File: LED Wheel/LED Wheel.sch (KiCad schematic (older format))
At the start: 0 parts

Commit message: Init Commit
Initial Commit with the Near-Finished Board Layout
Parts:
- added H1, H2, H3: MountingHole, MountingHole:MountingHole_2.2mm_M2, symbol Mechanical:MountingHole
- added J1, J2, J3: I/O, Connector_PinHeader_1.27mm:PinHeader_1x08_P1.27mm_Vertical, symbol Connector_Generic:Conn_01x08
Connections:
- new net +12V: J1.1 (Pin_1), J2.1 (Pin_1), J3.1 (Pin_1)
- new net GND: J1.8 (Pin_8), J2.8 (Pin_8), J3.8 (Pin_8)
- new net SPI1_CLK: J1.5 (Pin_5), J2.5 (Pin_5), J3.5 (Pin_5)
- new net SPI1_MISO: J1.4 (Pin_4), J2.4 (Pin_4), J3.4 (Pin_4)
- new net SPI1_MOSI: J1.3 (Pin_3), J2.3 (Pin_3), J3.3 (Pin_3)
- new net ~0E~: J1.6 (Pin_6), J2.6 (Pin_6), J3.6 (Pin_6)
- new net ~CS~_BLUE: J1.2 (Pin_2)
- new net ~CS~_GREEN: J3.2 (Pin_2)
- new net ~CS~_RED: J2.2 (Pin_2)
- new net ~RESET~: J1.7 (Pin_7), J2.7 (Pin_7), J3.7 (Pin_7)

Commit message: Rev A0 Commit
Files all sent to PCB manufacturer & BOM
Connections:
- net ~CS~_GREEN is gone; now on net Blue LED Controller/~OE~: J3.2 (Pin_2)
- net ~CS~_RED is gone; now on net Blue LED Controller/~OE~: J2.2 (Pin_2)
- net SPI1_CLK renamed Blue LED Controller/SPI1_CLK
- net SPI1_MISO renamed Blue LED Controller/~RESET~
- removed net SPI1_MOSI: J1.3 (Pin_3), J2.3 (Pin_3), J3.3 (Pin_3)
- net ~0E~ renamed Blue LED Controller/SPI1_MOSI
- net ~CS~_BLUE renamed Blue LED Controller/~OE~
- net ~RESET~ renamed Blue LED Controller/SPI1_MISO
- new net Blue LED Controller/~CS~_BLUE: J1.3 (Pin_3)
- new net Green LED Controller/~CS~_GREEN: J3.3 (Pin_3)
- new net Red LED Controller/~CS~_RED: J2.3 (Pin_3)
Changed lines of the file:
@@
 F0 "Green LED Controller" 50
 F1 "G_LED_Controller.sch" 50
-F2 "SPI1_MOSI" I L 4500 6050 50
+F2 "SPI1_MOSI" I L 4500 6350 50
 F3 "SPI1_CLK" I L 4500 6250 50
-F4 "~OE~" I L 4500 6350 50
-F5 "~RESET~" I L 4500 6450 50
-F6 "SPI1_MISO" O L 4500 6150 50
-F7 "~CS~_GREEN" I L 4500 5950 50
+F4 "~OE~" I L 4500 5950 50
+F5 "~RESET~" I L 4500 6150 50
+F6 "SPI1_MISO" O L 4500 6450 50
+F7 "~CS~_GREEN" I L 4500 6050 50
 F8 "G_12V" I L 4500 5725 50
 F9 "G_GND" I L 4500 6675 50
@@
 F0 "Red LED Controller" 50
 F1 "R_LED_Controller.sch" 50
-F2 "SPI1_MOSI" I L 4525 4400 50
+F2 "SPI1_MOSI" I L 4525 4700 50
 F3 "SPI1_CLK" I L 4525 4600 50
-F4 "~OE~" I L 4525 4700 50
-F5 "~RESET~" I L 4525 4800 50
-F6 "SPI1_MISO" O L 4525 4500 50
-F7 "~CS~_RED" I L 4525 4300 50
+F4 "~OE~" I L 4525 4300 50
+F5 "~RESET~" I L 4525 4500 50
+F6 "SPI1_MISO" O L 4525 4800 50
+F7 "~CS~_RED" I L 4525 4400 50
 F8 "R_GND" I L 4525 5025 50
 F9 "R_12V" I L 4525 4075 50
@@
 Wire Wire Line
 	4200 3400 4525 3400
-Wire Wire Line
-	2850 2675 2950 2675
-Wire Wire Line
-	2850 2775 3425 2775
-Wire Wire Line
-	2850 2875 3500 2875
-Wire Wire Line
-	2850 2975 3575 2975
-Wire Wire Line
-	2850 3075 3650 3075
-Wire Wire Line
-	2850 3175 3725 3175
 Wire Wire Line
 	4200 3400 4200 3275
@@
 F0 "Blue LED Controller" 50
 F1 "B_LED_Controller.sch" 50
-F2 "~CS~_BLUE" I L 4525 2675 50
-F3 "SPI1_MOSI" I L 4525 2775 50
+F2 "~CS~_BLUE" I L 4525 2775 50
+F3 "SPI1_MOSI" I L 4525 3075 50
 F4 "SPI1_CLK" I L 4525 2975 50
-F5 "~OE~" I L 4525 3075 50
-F6 "~RESET~" I L 4525 3175 50
-F7 "SPI1_MISO" O L 4525 2875 50
+F5 "~OE~" I L 4525 2675 50
+F6 "~RESET~" I L 4525 2875 50
+F7 "SPI1_MISO" O L 4525 3175 50
 F8 "B_12V" I L 4525 2450 50
 F9 "B_GND" I L 4525 3400 50
@@
 $EndComp
 Wire Wire Line
-	2850 4300 2950 4300
-Wire Wire Line
-	4525 4400 3425 4400
-Wire Wire Line
-	2850 4500 3500 4500
-Wire Wire Line
-	2850 4600 3575 4600
-Wire Wire Line
-	4525 4700 3650 4700
-Wire Wire Line
-	4525 4800 3725 4800
-Wire Wire Line
-	2850 4900 4200 4900
-Wire Wire Line
 	4200 5025 4525 5025
 Wire Wire Line
@@
 $EndComp
 Wire Wire Line
-	2825 5950 2950 5950
-Wire Wire Line
-	4500 6050 3425 6050
-Wire Wire Line
-	2825 6150 3500 6150
-Wire Wire Line
-	2825 6250 3575 6250
-Wire Wire Line
-	4500 6350 3650 6350
-Wire Wire Line
-	4500 6450 3725 6450
-Wire Wire Line
 	2825 6550 4175 6550
 Wire Wire Line
@@
 	4175 5625 4175 5725
 Connection ~ 4175 5725
-Wire Wire Line
-	3425 2775 3425 4400
-Connection ~ 3425 2775
-Wire Wire Line
-	3425 2775 4525 2775
-Connection ~ 3425 4400
-Wire Wire Line
-	3425 4400 2850 4400
-Wire Wire Line
-	3425 4400 3425 6050
-Connection ~ 3425 6050
-Wire Wire Line
-	3425 6050 2825 6050
-Wire Wire Line
-	3500 2875 3500 4500
-Connection ~ 3500 2875
-Wire Wire Line
-	3500 2875 4525 2875
-Connection ~ 3500 4500
-Wire Wire Line
-	3500 4500 4525 4500
-Wire Wire Line
-	3500 4500 3500 6150
-Connection ~ 3500 6150
-Wire Wire Line
-	3500 6150 4500 6150
-Wire Wire Line
-	3575 2975 3575 4600
-Connection ~ 3575 2975
-Wire Wire Line
-	3575 2975 4525 2975
-Connection ~ 3575 4600
-Wire Wire Line
-	3575 4600 4525 4600
-Wire Wire Line
-	3575 4600 3575 6250
-Connection ~ 3575 6250
-Wire Wire Line
-	3575 6250 4500 6250
-Wire Wire Line
-	3650 3075 3650 4700
-Connection ~ 3650 3075
-Wire Wire Line
-	3650 3075 4525 3075
-Connection ~ 3650 4700
-Wire Wire Line
-	3650 4700 2850 4700
-Wire Wire Line
-	3650 4700 3650 6350
-Connection ~ 3650 6350
-Wire Wire Line
-	3650 6350 2825 6350
-Wire Wire Line
-	3725 3175 3725 4800
-Connection ~ 3725 3175
-Wire Wire Line
-	3725 3175 4525 3175
-Connection ~ 3725 4800
-Wire Wire Line
-	3725 4800 2850 4800
-Wire Wire Line
-	3725 4800 3725 6450
-Connection ~ 3725 6450
-Wire Wire Line
-	3725 6450 2825 6450
-Text GLabel 2775 3425 0    50   Input ~ 0
-~CS~_BLUE
-Wire Wire Line
-	2775 3425 2950 3425
-Wire Wire Line
-	2950 3425 2950 2675
-Connection ~ 2950 2675
-Wire Wire Line
-	2950 2675 4525 2675
-Text GLabel 2775 5050 0    50   Input ~ 0
-~CS~_RED
-Wire Wire Line
-	2775 5050 2950 5050
-Wire Wire Line
-	2950 5050 2950 4300
-Connection ~ 2950 4300
-Wire Wire Line
-	2950 4300 4525 4300
-Text GLabel 2775 6700 0    50   Input ~ 0
-~CS~_GREEN
-Wire Wire Line
-	2775 6700 2950 6700
-Wire Wire Line
-	2950 6700 2950 5950
-Text GLabel 3025 2250 0    50   Input ~ 0
-SPI1_MOSI
-Wire Wire Line
-	3025 2250 3425 2250
-Wire Wire Line
-	3425 2250 3425 2775
-Text GLabel 3025 2150 0    50   Input ~ 0
-SPI1_MISO
-Wire Wire Line
-	3025 2150 3500 2150
-Wire Wire Line
-	3500 2150 3500 2875
-Connection ~ 2950 5950
-Wire Wire Line
-	2950 5950 4500 5950
-Text GLabel 3025 2050 0    50   Input ~ 0
-SPI1_CLK
-Text GLabel 3025 1950 0    35   Input ~ 0
-~0E~
-Text GLabel 3025 1850 0    35   Input ~ 0
-~RESET~
-Wire Wire Line
-	3025 1850 3725 1850
-Wire Wire Line
-	3725 1850 3725 3175
-Wire Wire Line
-	3650 3075 3650 1950
-Wire Wire Line
-	3650 1950 3025 1950
-Wire Wire Line
-	3025 2050 3575 2050
-Wire Wire Line
-	3575 2050 3575 2975
 $Comp
 L Mechanical:MountingHole H1
@@
 	1    0    0    -1
 $EndComp
+Wire Wire Line
+	2850 4900 4200 4900
+Wire Wire Line
+	2850 2775 4525 2775
+Wire Wire Line
+	2850 4400 4525 4400
+Wire Wire Line
+	2825 6050 4500 6050
+Wire Wire Line
+	3575 6250 4500 6250
+Wire Wire Line
+	2825 6250 3575 6250
+Connection ~ 3575 6250
+Wire Wire Line
+	2850 4600 3575 4600
+Wire Wire Line
+	3575 4600 4525 4600
+Connection ~ 3575 4600
+Wire Wire Line
+	3575 4600 3575 6250
+Wire Wire Line
+	3500 6150 4500 6150
+Wire Wire Line
+	2825 6150 3500 6150
+Connection ~ 3500 6150
+Wire Wire Line
+	3500 4500 4525 4500
+Wire Wire Line
+	2850 4500 3500 4500
+Connection ~ 3500 4500
+Wire Wire Line
+	3500 4500 3500 6150
+Wire Wire Line
+	3725 6450 4500 6450
+Wire Wire Line
+	2825 6450 3725 6450
+Connection ~ 3725 6450
+Wire Wire Line
+	3725 4800 4525 4800
+Wire Wire Line
+	2850 4800 3725 4800
+Connection ~ 3725 4800
+Wire Wire Line
+	3725 4800 3725 6450
+Wire Wire Line
+	3650 6350 4500 6350
+Wire Wire Line
+	2825 6350 3650 6350
+Connection ~ 3650 6350
+Wire Wire Line
+	2850 4700 3650 4700
+Wire Wire Line
+	3650 4700 4525 4700
+Connection ~ 3650 4700
+Wire Wire Line
+	3650 4700 3650 6350
+Wire Wire Line
+	3425 5950 4500 5950
+Wire Wire Line
+	2825 5950 3425 5950
+Connection ~ 3425 5950
+Wire Wire Line
+	3425 4300 4525 4300
+Wire Wire Line
+	2850 4300 3425 4300
+Connection ~ 3425 4300
+Wire Wire Line
+	3425 4300 3425 5950
+Wire Wire Line
+	3575 2975 4525 2975
+Wire Wire Line
+	2850 2975 3575 2975
+Connection ~ 3575 2975
+Wire Wire Line
+	3575 2975 3575 4600
+Wire Wire Line
+	3500 2875 4525 2875
+Wire Wire Line
+	2850 2875 3500 2875
+Connection ~ 3500 2875
+Wire Wire Line
+	3500 2875 3500 4500
+Wire Wire Line
+	3725 3175 4525 3175
+Wire Wire Line
+	2850 3175 3725 3175
+Connection ~ 3725 3175
+Wire Wire Line
+	3725 3175 3725 4800
+Wire Wire Line
+	2850 3075 3650 3075
+Wire Wire Line
+	3650 3075 4525 3075
+Connection ~ 3650 3075
+Wire Wire Line
+	3650 3075 3650 4700
+Wire Wire Line
+	3425 2675 4525 2675
+Wire Wire Line
+	2850 2675 3425 2675
+Connection ~ 3425 2675
+Wire Wire Line
+	3425 2675 3425 4300
 $EndSCHEMATC

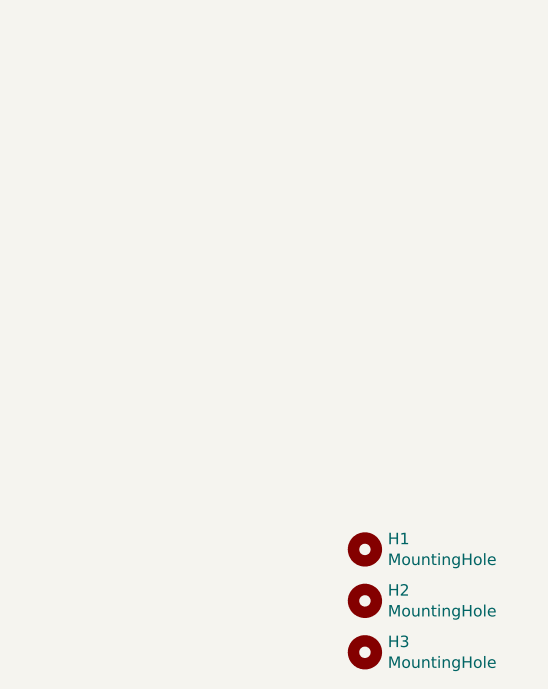
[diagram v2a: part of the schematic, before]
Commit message: Updated LED Wheel for PCBWay
Added Light reflector for speed sensor, updated board layout for VCut
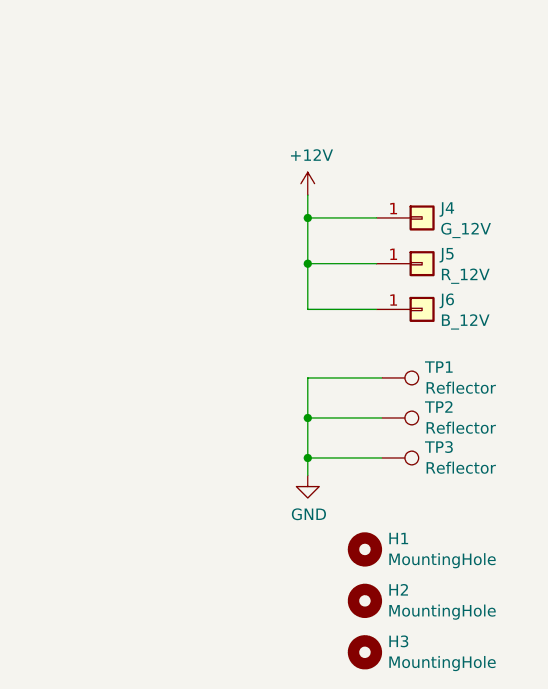
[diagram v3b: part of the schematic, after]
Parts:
- added J4: G_12V, Connector_PinHeader_2.54mm:PinHeader_1x01_P2.54mm_Vertical, symbol Connector_Generic:Conn_01x01
- added J5: R_12V, Connector_PinHeader_2.54mm:PinHeader_1x01_P2.54mm_Vertical, symbol Connector_Generic:Conn_01x01
- added J6: B_12V, Connector_PinHeader_2.54mm:PinHeader_1x01_P2.54mm_Vertical, symbol Connector_Generic:Conn_01x01
- added TP1, TP2, TP3: Reflector, Project_Library:Reflector 2x4mm, symbol Connector:TestPoint
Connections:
- net +12V: now also J4.1 (Pin_1), J5.1 (Pin_1), J6.1 (Pin_1)
- net GND: now also TP1.1, TP2.1, TP3.1
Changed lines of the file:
@@
 Wire Wire Line
 	3425 2675 3425 4300
+$Comp
+L Connector_Generic:Conn_01x01 J4
+U 1 1 613F8E08
+P 8200 3000
+F 0 "J4" H 8280 3042 50  0000 L CNN
+F 1 "G_12V" H 8280 2951 50  0000 L CNN
+F 2 "Connector_PinHeader_2.54mm:PinHeader_1x01_P2.54mm_Vertical" H 8200 3000 50  0001 C CNN
+F 3 "~" H 8200 3000 50  0001 C CNN
+	1    8200 3000
+	1    0    0    -1
+$EndComp
+$Comp
+L Connector_Generic:Conn_01x01 J5
+U 1 1 613F9BBC
+P 8200 3200
+F 0 "J5" H 8280 3242 50  0000 L CNN
+F 1 "R_12V" H 8280 3151 50  0000 L CNN
+F 2 "Connector_PinHeader_2.54mm:PinHeader_1x01_P2.54mm_Vertical" H 8200 3200 50  0001 C CNN
+F 3 "~" H 8200 3200 50  0001 C CNN
+	1    8200 3200
+	1    0    0    -1
+$EndComp
+$Comp
+L Connector_Generic:Conn_01x01 J6
+U 1 1 613FA00C
+P 8200 3400
+F 0 "J6" H 8280 3442 50  0000 L CNN
+F 1 "B_12V" H 8280 3351 50  0000 L CNN
+F 2 "Connector_PinHeader_2.54mm:PinHeader_1x01_P2.54mm_Vertical" H 8200 3400 50  0001 C CNN
+F 3 "~" H 8200 3400 50  0001 C CNN
+	1    8200 3400
+	1    0    0    -1
+$EndComp
+$Comp
+L power:+12V #PWR0101
+U 1 1 613FBD9A
+P 7700 2900
+F 0 "#PWR0101" H 7700 2750 50  0001 C CNN
+F 1 "+12V" H 7715 3073 50  0000 C CNN
+F 2 "" H 7700 2900 50  0001 C CNN
+F 3 "" H 7700 2900 50  0001 C CNN
+	1    7700 2900
+	1    0    0    -1
+$EndComp
+Wire Wire Line
+	7700 2900 7700 3000
+Wire Wire Line
+	7700 3000 8000 3000
+Wire Wire Line
+	7700 3000 7700 3200
+Wire Wire Line
+	7700 3200 8000 3200
+Connection ~ 7700 3000
+Wire Wire Line
+	8000 3400 7700 3400
+Wire Wire Line
+	7700 3400 7700 3200
+Connection ~ 7700 3200
+$Comp
+L Connector:TestPoint TP1
+U 1 1 6140DAE7
+P 8025 3700
+F 0 "TP1" V 7979 3888 50  0000 L CNN
+F 1 "Reflector" V 8070 3888 50  0000 L CNN
+F 2 "Project_Library:Reflector 2x4mm" H 8225 3700 50  0001 C CNN
+F 3 "~" H 8225 3700 50  0001 C CNN
+	1    8025 3700
+	0    1    1    0
+$EndComp
+$Comp
+L Connector:TestPoint TP2
+U 1 1 6140E191
+P 8025 3875
+F 0 "TP2" V 7979 4063 50  0000 L CNN
+F 1 "Reflector" V 8070 4063 50  0000 L CNN
+F 2 "Project_Library:Reflector 2x4mm" H 8225 3875 50  0001 C CNN
+F 3 "~" H 8225 3875 50  0001 C CNN
+	1    8025 3875
+	0    1    1    0
+$EndComp
+$Comp
+L Connector:TestPoint TP3
+U 1 1 6140E405
+P 8025 4050
+F 0 "TP3" V 7979 4238 50  0000 L CNN
+F 1 "Reflector" V 8070 4238 50  0000 L CNN
+F 2 "Project_Library:Reflector 2x4mm" H 8225 4050 50  0001 C CNN
+F 3 "~" H 8225 4050 50  0001 C CNN
+	1    8025 4050
+	0    1    1    0
+$EndComp
+Wire Wire Line
+	8025 3700 7700 3700
+Wire Wire Line
+	8025 3875 7700 3875
+Wire Wire Line
+	7700 3875 7700 3700
+Wire Wire Line
+	8025 4050 7700 4050
+Wire Wire Line
+	7700 4050 7700 3875
+Connection ~ 7700 3875
+$Comp
+L power:GND #PWR?
+U 1 1 614231D6
+P 7700 4125
+F 0 "#PWR?" H 7700 3875 50  0001 C CNN
+F 1 "GND" H 7705 3952 50  0000 C CNN
+F 2 "" H 7700 4125 50  0001 C CNN
+F 3 "" H 7700 4125 50  0001 C CNN
+	1    7700 4125
+	1    0    0    -1
+$EndComp
+Wire Wire Line
+	7700 4125 7700 4050
+Connection ~ 7700 4050
 $EndSCHEMATC
